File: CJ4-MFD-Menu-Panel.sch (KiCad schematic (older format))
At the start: 50 parts, among them SW1 SW_Push_LED, SW10 5_Way_Switch, SW11 SW_Push_LED, SW12 SW_Push_LED, SW13 SW_Push_LED, SW14 SW_Push_LED, SW15 SW_Push_LED, SW16 SW_Push_LED, SW17 SW_Push_LED, SW18 SW_Push_LED, SW19 SW_Push_LED, SW2 SW_Push_LED, SW20 SW_Push_LED, SW21 SW_Push_LED, SW3 SW_Push_LED, SW4 SW_Push_LED, SW5 SW_Push_LED, SW6 SW_Push_LED, SW7 SW_Push_LED, SW8 SW_Push_LED, SW9 SW_Push_LED, U1 MCP23017_SO, U2 MCP23017_SO, U3 IS31FL3733B

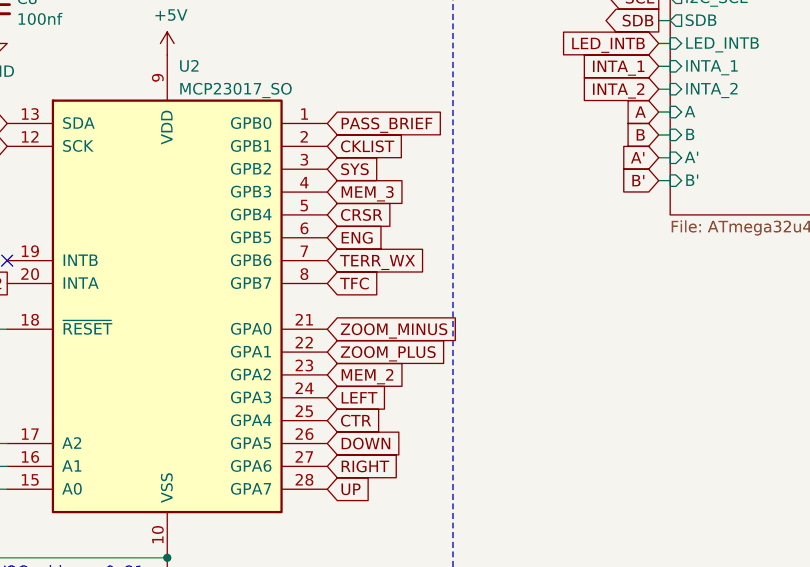
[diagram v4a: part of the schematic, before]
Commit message: Partiall routed but going to rip it all up and start over
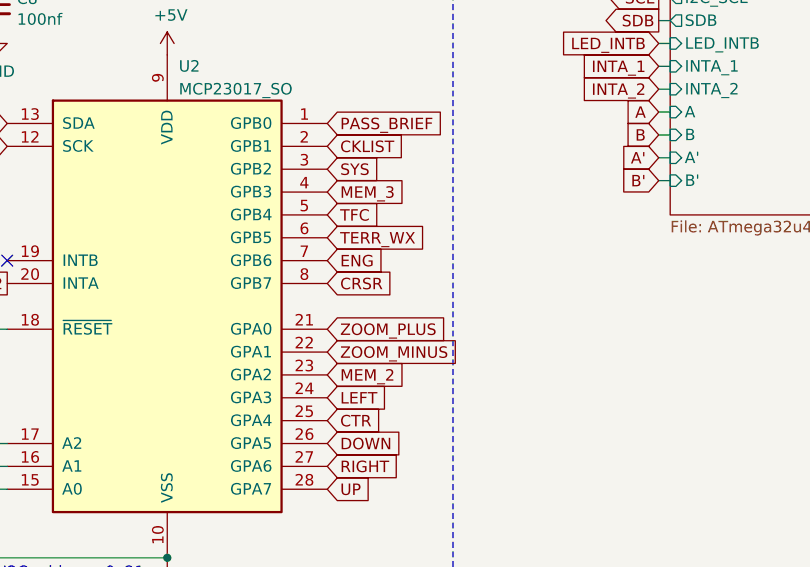
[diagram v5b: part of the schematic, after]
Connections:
- net CRSR: now also U2.8 (GPB7); no longer U2.5 (GPB4)
- net ENG: now also U2.7 (GPB6); no longer U2.6 (GPB5)
- net TERR_WX: now also U2.6 (GPB5); no longer U2.7 (GPB6)
- net TFC: now also U2.5 (GPB4); no longer U2.8 (GPB7)
- net ZOOM_MINUS: now also U2.22 (GPA1); no longer U2.21 (GPA0)
- net ZOOM_PLUS: now also U2.21 (GPA0); no longer U2.22 (GPA1)
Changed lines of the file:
@@
 Text GLabel 2500 6200 2    50   Input ~ 0
 LWR_MENU
-Text GLabel 5200 6000 2    50   Input ~ 0
+Text GLabel 5200 6300 2    50   Input ~ 0
 CRSR
-Text GLabel 5200 6100 2    50   Input ~ 0
+Text GLabel 5200 6200 2    50   Input ~ 0
 ENG
 Text GLabel 2500 6600 2    50   Input ~ 0
 ESC
-Text GLabel 5200 6200 2    50   Input ~ 0
+Text GLabel 5200 6100 2    50   Input ~ 0
 TERR_WX
 Text GLabel 2500 6700 2    50   Input ~ 0
 DATABASE
-Text GLabel 5200 6300 2    50   Input ~ 0
+Text GLabel 5200 6000 2    50   Input ~ 0
 TFC
 Text GLabel 2500 6800 2    50   Input ~ 0
@@
 Text GLabel 2500 6100 2    50   Input ~ 0
 RADAR_MENU
-Text GLabel 5200 6500 2    50   Input ~ 0
+Text GLabel 5200 6600 2    50   Input ~ 0
 ZOOM_MINUS
 Text GLabel 5200 5800 2    50   Input ~ 0
@@
 Text GLabel 2500 7000 2    50   Input ~ 0
 CAS_PAGE
-Text GLabel 5200 6600 2    50   Input ~ 0
+Text GLabel 5200 6500 2    50   Input ~ 0
 ZOOM_PLUS
 Text GLabel 5200 5700 2    50   Input ~ 0

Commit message: Fully routed and ready to go
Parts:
- removed C1, C2, C3, C4: 0.01uf, CJ4-MFD-Menu-Panel:Perfect_0402, symbol Device:C_Small
- removed R5, R6, R7, R8: 10k, CJ4-MFD-Menu-Panel:Perfect_0402, symbol Device:R_Small
- added H1, H2, H3, H4: MountingHole, MountingHole:MountingHole_3.2mm_M3, symbol Mechanical:MountingHole
- added H5, H6, H7: JLCPCB, CJ4-MFD-Menu-Panel:JLCPCB_Tooling_Hole, symbol Mechanical:MountingHole
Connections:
- net CAS_PAGE: now also U1.7 (GPB6); no longer U1.26 (GPA5)
- net CHART: now also U1.8 (GPB7); no longer U1.25 (GPA4)
- net CKLIST: now also U2.24 (GPA3); no longer U2.2 (GPB1)
- net CRSR: now also U2.21 (GPA0); no longer U2.8 (GPB7)
- net CTR: no longer U2.25 (GPA4)
- net DATABASE: now also U1.5 (GPB4); no longer U1.23 (GPA2)
- net DOWN: no longer U2.26 (GPA5)
- net ENG: now also U2.28 (GPA7); no longer U2.7 (GPB6)
- net ESC: now also U1.4 (GPB3); no longer U1.22 (GPA1)
- net E_BTN: now also U1.21 (GPA0); no longer U1.8 (GPB7)
- net LEFT: no longer U2.24 (GPA3)
- net LWR_MENU: now also U1.28 (GPA7); no longer U1.7 (GPB6)
- net MEM_1: now also U1.27 (GPA6); no longer U1.5 (GPB4)
- net MEM_2: now also U2.5 (GPB4); no longer U2.23 (GPA2)
- net MEM_3: now also U2.25 (GPA4); no longer U2.4 (GPB3)
- net NAV_DATA: now also U1.6 (GPB5); no longer U1.24 (GPA3)
- net PASS_BRIEF: now also U2.22 (GPA1); no longer U2.1 (GPB0)
- net RADAR_MENU: now also U1.26 (GPA5); no longer U1.6 (GPB5)
- net RIGHT: no longer U2.27 (GPA6)
- net SYS: now also U2.23 (GPA2); no longer U2.3 (GPB2)
- net TERR_WX: now also U2.27 (GPA6); no longer U2.6 (GPB5)
- net TFC: now also U2.26 (GPA5); no longer U2.5 (GPB4)
- net UP: no longer U2.28 (GPA7)
- net UPR_MENU: now also U1.3 (GPB2); no longer U1.21 (GPA0)
- net ZOOM_MINUS: now also U2.4 (GPB3); no longer U2.22 (GPA1)
- net ZOOM_PLUS: now also U2.3 (GPB2); no longer U2.21 (GPA0)
- no-connect marks 26 -> 31
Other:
- note added: "Microcontroller and power"

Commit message: Miscellaneous fixes
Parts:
- C10, C11, C12, C13, C14, C15, C5, C6, C7, C8, C9: JLC (none) -> 0402
- R1, R2, R3, R4: JLC (none) -> 0402; LCSC (none) -> C25744
- R10: JLC (none) -> 0402; LCSC (none) -> C25792
- R9: JLC (none) -> 0402; LCSC (none) -> C25741
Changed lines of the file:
@@
 F 2 "CJ4-MFD-Menu-Panel:Perfect_0402" H 1000 3550 50  0001 C CNN
 F 3 "~" H 1000 3550 50  0001 C CNN
+F 4 "0402" H 1000 3550 50  0001 C CNN "JLC"
+F 5 "C25744" H 1000 3550 50  0001 C CNN "LCSC"
 	1    1000 3550
 	1    0    0    -1
@@
 F 2 "CJ4-MFD-Menu-Panel:Perfect_0402" H 1450 3450 50  0001 C CNN
 F 3 "~" H 1450 3450 50  0001 C CNN
+F 4 "0402" H 1450 3450 50  0001 C CNN "JLC"
+F 5 "C25744" H 1450 3450 50  0001 C CNN "LCSC"
 	1    1450 3450
 	1    0    0    -1
@@
 F 2 "CJ4-MFD-Menu-Panel:Perfect_0402" H 1050 5100 50  0001 C CNN
 F 3 "~" H 1050 5100 50  0001 C CNN
+F 4 "0402" H 1050 5100 50  0001 C CNN "JLC"
 	1    1050 5100
 	1    0    0    -1
@@
 F 2 "CJ4-MFD-Menu-Panel:Perfect_0402" H 700 5100 50  0001 C CNN
 F 3 "~" H 700 5100 50  0001 C CNN
+F 4 "0402" H 700 5100 50  0001 C CNN "JLC"
 	1    700  5100
 	1    0    0    -1
@@
 F 2 "CJ4-MFD-Menu-Panel:Perfect_0402" H 3750 5100 50  0001 C CNN
 F 3 "~" H 3750 5100 50  0001 C CNN
+F 4 "0402" H 3750 5100 50  0001 C CNN "JLC"
 	1    3750 5100
 	1    0    0    -1
@@
 F 2 "CJ4-MFD-Menu-Panel:Perfect_0402" H 3400 5100 50  0001 C CNN
 F 3 "~" H 3400 5100 50  0001 C CNN
+F 4 "0402" H 3400 5100 50  0001 C CNN "JLC"
 	1    3400 5100
 	1    0    0    -1
@@
 F 2 "CJ4-MFD-Menu-Panel:Perfect_0402" H 9650 4800 50  0001 C CNN
 F 3 "~" H 9650 4800 50  0001 C CNN
+F 4 "0402" H 9650 4800 50  0001 C CNN "JLC"
+F 5 "C25792" H 9650 4800 50  0001 C CNN "LCSC"
 	1    9650 4800
 	1    0    0    -1
@@
 F 2 "CJ4-MFD-Menu-Panel:Perfect_0402" H 9650 4250 50  0001 C CNN
 F 3 "~" H 9650 4250 50  0001 C CNN
+F 4 "0402" H 9650 4250 50  0001 C CNN "JLC"
 	1    9650 4250
 	1    0    0    -1
@@
 F 2 "CJ4-MFD-Menu-Panel:Perfect_0402" H 9300 3950 50  0001 C CNN
 F 3 "~" H 9300 3950 50  0001 C CNN
+F 4 "0402" H 9300 3950 50  0001 C CNN "JLC"
+F 5 "C25741" H 9300 3950 50  0001 C CNN "LCSC"
 	1    9300 3950
 	1    0    0    -1
@@
 F 2 "CJ4-MFD-Menu-Panel:Perfect_0402" H 9650 2300 50  0001 C CNN
 F 3 "~" H 9650 2300 50  0001 C CNN
+F 4 "0402" H 9650 2300 50  0001 C CNN "JLC"
 	1    9650 2300
 	1    0    0    -1
@@
 F 2 "CJ4-MFD-Menu-Panel:Perfect_0402" H 9200 2300 50  0001 C CNN
 F 3 "~" H 9200 2300 50  0001 C CNN
+F 4 "0402" H 9200 2300 50  0001 C CNN "JLC"
 	1    9200 2300
 	1    0    0    -1
@@
 F 2 "CJ4-MFD-Menu-Panel:Perfect_0402" H 9650 2600 50  0001 C CNN
 F 3 "~" H 9650 2600 50  0001 C CNN
+F 4 "0402" H 9650 2600 50  0001 C CNN "JLC"
 	1    9650 2600
 	1    0    0    -1
@@
 F 2 "CJ4-MFD-Menu-Panel:Perfect_0402" H 9200 2600 50  0001 C CNN
 F 3 "~" H 9200 2600 50  0001 C CNN
+F 4 "0402" H 9200 2600 50  0001 C CNN "JLC"
 	1    9200 2600
 	1    0    0    -1
@@
 F 2 "CJ4-MFD-Menu-Panel:Perfect_0402" H 9650 2950 50  0001 C CNN
 F 3 "~" H 9650 2950 50  0001 C CNN
+F 4 "0402" H 9650 2950 50  0001 C CNN "JLC"
 	1    9650 2950
 	1    0    0    -1
@@
 F 2 "CJ4-MFD-Menu-Panel:Perfect_0402" H 9200 2950 50  0001 C CNN
 F 3 "~" H 9200 2950 50  0001 C CNN
+F 4 "0402" H 9200 2950 50  0001 C CNN "JLC"
 	1    9200 2950
 	1    0    0    -1
@@
 F 2 "CJ4-MFD-Menu-Panel:Perfect_0402" H 1900 3250 50  0001 C CNN
 F 3 "~" H 1900 3250 50  0001 C CNN
+F 4 "0402" H 1900 3250 50  0001 C CNN "JLC"
+F 5 "C25744" H 1900 3250 50  0001 C CNN "LCSC"
 	1    1900 3250
 	1    0    0    -1
@@
 F 2 "CJ4-MFD-Menu-Panel:Perfect_0402" H 2350 3150 50  0001 C CNN
 F 3 "~" H 2350 3150 50  0001 C CNN
+F 4 "0402" H 2350 3150 50  0001 C CNN "JLC"
+F 5 "C25744" H 2350 3150 50  0001 C CNN "LCSC"
 	1    2350 3150
 	1    0    0    -1

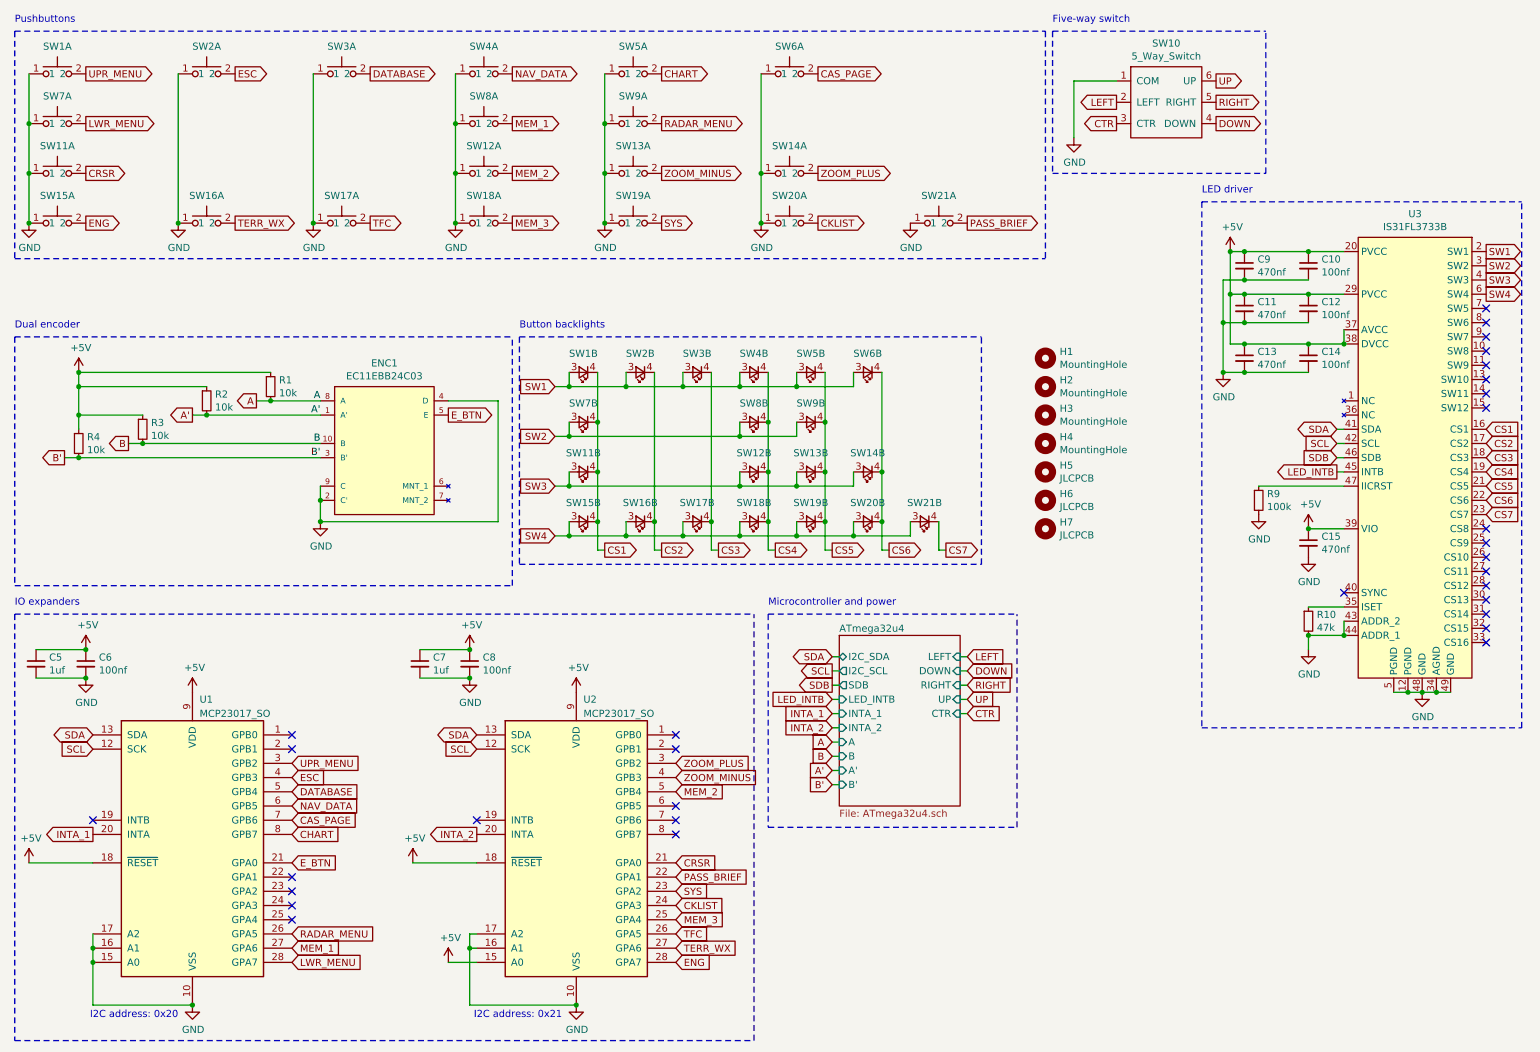
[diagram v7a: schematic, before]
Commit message: Clean up schematic Fixes #13
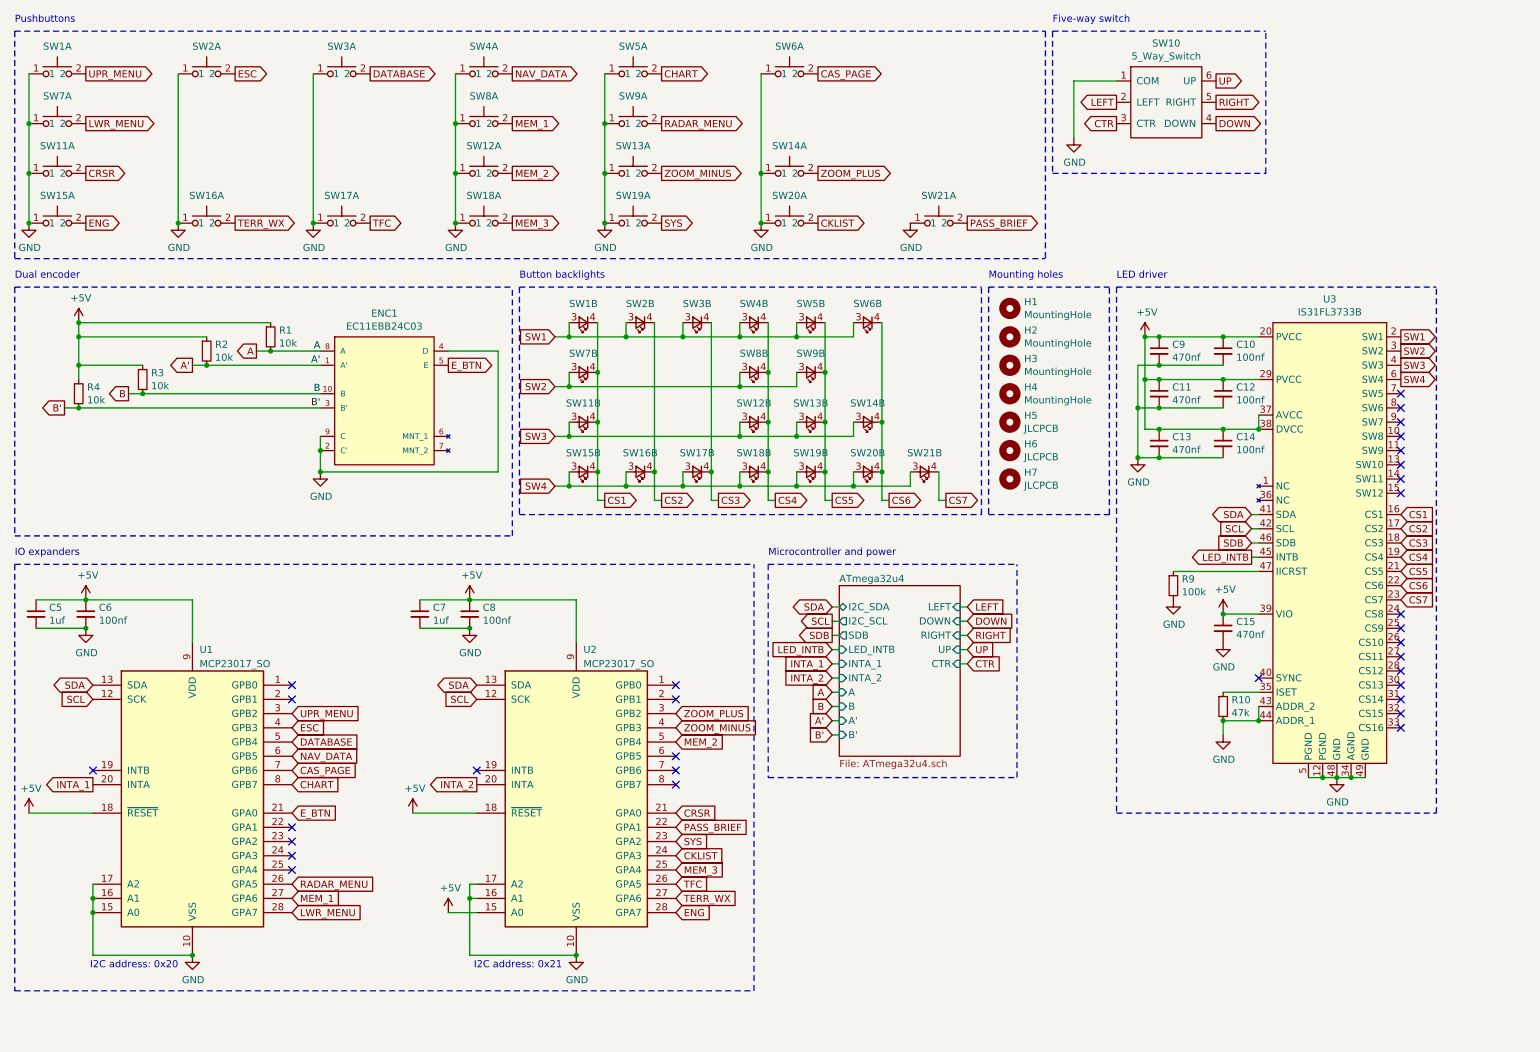
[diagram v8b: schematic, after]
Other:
- note added: "Mounting holes"
- moved on the sheet: C10, C11, C12, C13, C14, C15, C5, C6, C7, C8, C9, ENC1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
